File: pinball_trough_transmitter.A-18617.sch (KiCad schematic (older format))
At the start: 8 parts, among them J1 Conn_01x09_Male

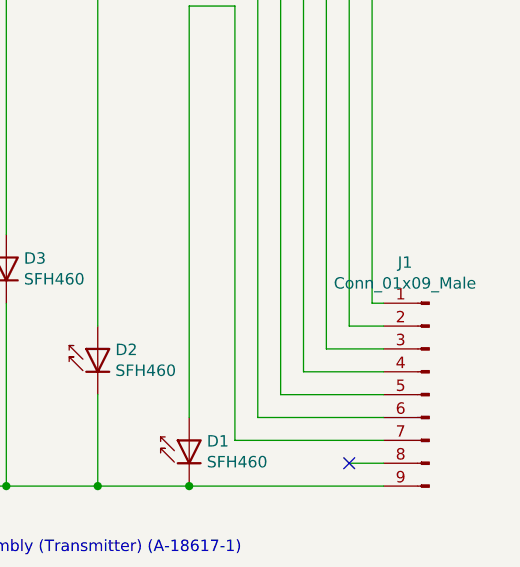
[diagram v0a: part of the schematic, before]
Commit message: Use Molex connector
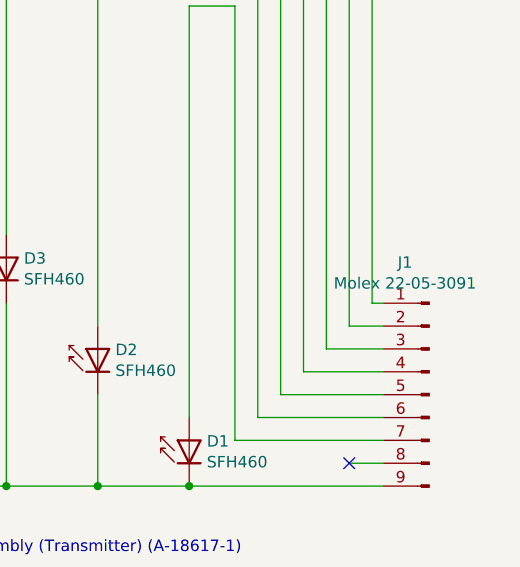
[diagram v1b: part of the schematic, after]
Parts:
- J1: value Conn_01x09_Male -> Molex 22-05-3091
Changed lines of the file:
@@
 P 7500 4700
 F 0 "J1" H 7606 5278 50  0000 C CNN
-F 1 "Conn_01x09_Male" H 7606 5187 50  0000 C CNN
+F 1 "Molex 22-05-3091" H 7606 5187 50  0000 C CNN
 F 2 "Connector_Molex:Molex_KK-254_AE-6410-09A_1x09_P2.54mm_Vertical" H 7500 4700 50  0001 C CNN
 F 3 "~" H 7500 4700 50  0001 C CNN
